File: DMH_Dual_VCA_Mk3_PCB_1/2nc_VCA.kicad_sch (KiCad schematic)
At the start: 51 parts, among them Q5 BC548, Q6 BC548, Q7 BC548, Q8 BC548, SW2 SW_DPDT_3way, U3 TL074, U4 TL072, U7 TL074

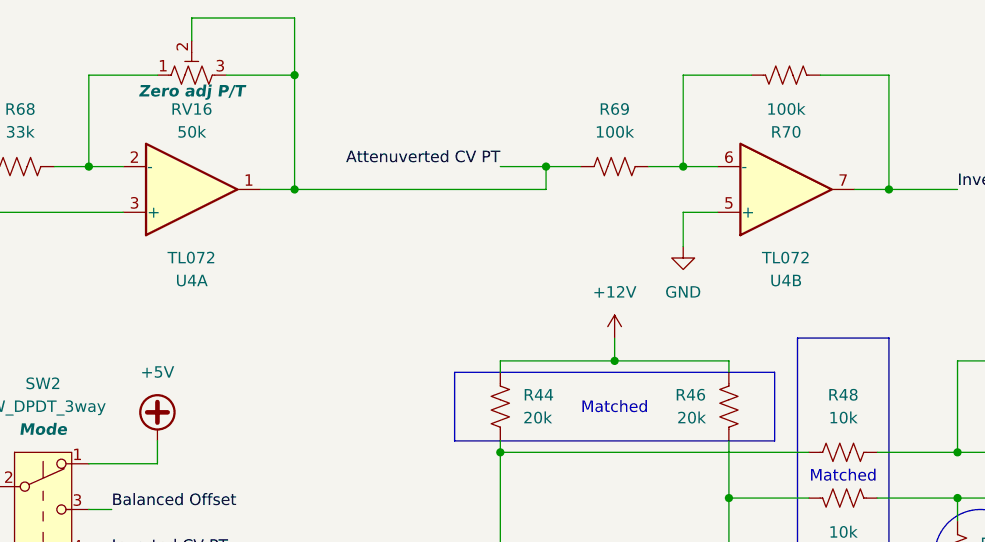
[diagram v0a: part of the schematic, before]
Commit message: Added clipping LED to schematic
Still need to add to Panel
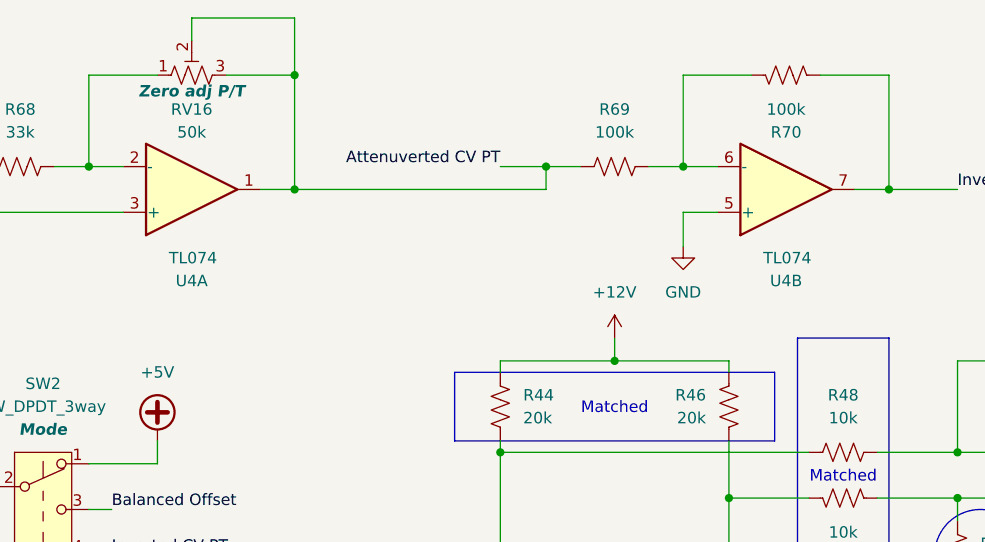
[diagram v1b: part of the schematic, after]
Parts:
- U4: value TL072 -> TL074; footprint Package_DIP:DIP-8_W7.62mm_Socket -> Package_DIP:DIP-14_W7.62mm_Socket; symbol Amplifier_Operational:TL072 -> Amplifier_Operational:TL074
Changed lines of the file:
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@@
 	)
 	(symbol
-		(lib_id "Amplifier_Operational:TL072")
+		(lib_id "Amplifier_Operational:TL074")
 		(at 54.61 31.75 0)
 		(mirror x)
@@
 		(exclude_from_sim no)
 		(in_bom yes)
-		(on_board no)
+		(on_board yes)
 		(dnp no)
 		(property "Reference" "U4"
@@
 			)
 		)
-		(property "Value" "TL072"
-			(at 54.61 39.37 0)
-			(effects
-				(font
-					(size 1.27 1.27)
-				)
-			)
-		)
-		(property "Footprint" "Package_DIP:DIP-8_W7.62mm_Socket"
+		(property "Value" "TL074"
+			(at 52.07 39.37 0)
+			(effects
+				(font
+					(size 1.27 1.27)
+				)
+				(justify left)
+			)
+		)
+		(property "Footprint" "Package_DIP:DIP-14_W7.62mm_Socket"
+			(at 53.34 34.29 0)
+			(effects
+				(font
+					(size 1.27 1.27)
+				)
+				(hide yes)
+			)
+		)
+		(property "Datasheet" "http://www.ti.com/lit/ds/symlink/tl071.pdf"
+			(at 55.88 36.83 0)
+			(effects
+				(font
+					(size 1.27 1.27)
+				)
+				(hide yes)
+			)
+		)
+		(property "Description" "Quad Low-Noise JFET-Input Operational Amplifiers, DIP-14/SOIC-14"
 			(at 54.61 31.75 0)
 			(effects
@@
 			)
 		)
-		(property "Datasheet" "http://www.ti.com/lit/ds/symlink/tl071.pdf"
+		(property "Function" ""
 			(at 54.61 31.75 0)
 			(effects
@@
 					(size 1.27 1.27)
 				)
-				(hide yes)
-			)
-		)
-		(property "Description" "Dual Low-Noise JFET-Input Operational Amplifiers, DIP-8/SOIC-8"
-			(at 54.61 31.75 0)
-			(effects
-				(font
-					(size 1.27 1.27)
-				)
-				(hide yes)
 			)
 		)
@@
 		)
 		(pin "4"
+		)
+		(pin "9"
+		)
+		(pin "10"
+		)
+		(pin "12"
+		)
+		(pin "13"
+		)
+		(pin "14"
+		)
+		(pin "11"
 		)
 		(instances
@@
 	)
 	(symbol
-		(lib_id "Amplifier_Operational:TL072")
+		(lib_id "Amplifier_Operational:TL074")
 		(at 120.65 31.75 0)
 		(mirror x)
@@
 		(exclude_from_sim no)
 		(in_bom yes)
-		(on_board no)
+		(on_board yes)
 		(dnp no)
 		(property "Reference" "U4"
@@
 			)
 		)
-		(property "Value" "TL072"
-			(at 120.65 39.37 0)
-			(effects
-				(font
-					(size 1.27 1.27)
-				)
-			)
-		)
-		(property "Footprint" "Package_DIP:DIP-8_W7.62mm_Socket"
+		(property "Value" "TL074"
+			(at 118.11 39.37 0)
+			(effects
+				(font
+					(size 1.27 1.27)
+				)
+				(justify left)
+			)
+		)
+		(property "Footprint" "Package_DIP:DIP-14_W7.62mm_Socket"
+			(at 119.38 34.29 0)
+			(effects
+				(font
+					(size 1.27 1.27)
+				)
+				(hide yes)
+			)
+		)
+		(property "Datasheet" "http://www.ti.com/lit/ds/symlink/tl071.pdf"
+			(at 121.92 36.83 0)
+			(effects
+				(font
+					(size 1.27 1.27)
+				)
+				(hide yes)
+			)
+		)
+		(property "Description" "Quad Low-Noise JFET-Input Operational Amplifiers, DIP-14/SOIC-14"
 			(at 120.65 31.75 0)
 			(effects
@@
 			)
 		)
-		(property "Datasheet" "http://www.ti.com/lit/ds/symlink/tl071.pdf"
+		(property "Function" ""
 			(at 120.65 31.75 0)
 			(effects
@@
 					(size 1.27 1.27)
 				)
-				(hide yes)
-			)
-		)
-		(property "Description" "Dual Low-Noise JFET-Input Operational Amplifiers, DIP-8/SOIC-8"
-			(at 120.65 31.75 0)
-			(effects
-				(font
-					(size 1.27 1.27)
-				)
-				(hide yes)
 			)
 		)
@@
 		(pin "4"
 		)
-		(instances
+		(pin "13"
+		)
+		(pin "14"
+		)
+		(pin "10"
+		)
+		(pin "9"
+		)
+		(pin "12"
+		)
+		(pin "11"
+		)
+		(instances

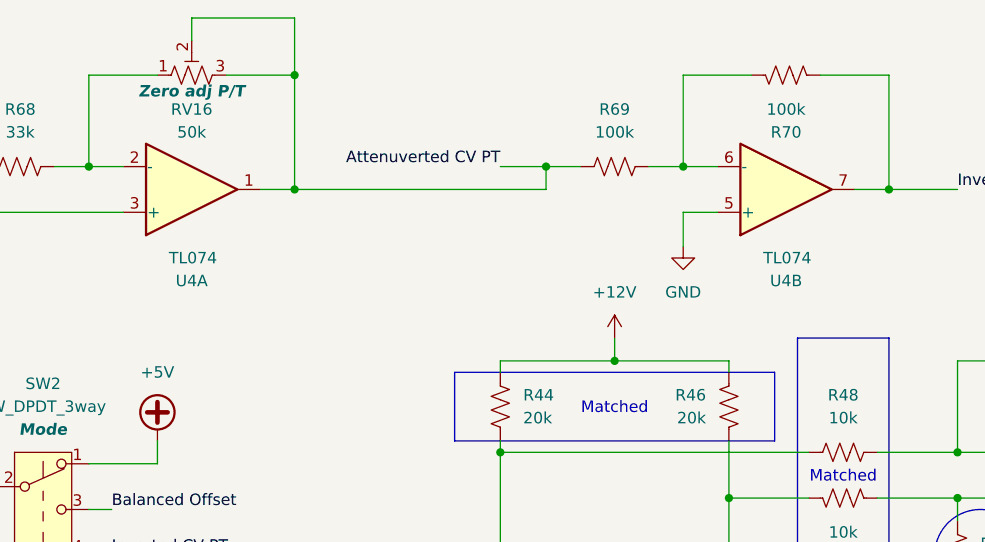
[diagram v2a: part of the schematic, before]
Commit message: Improved clipping indicator
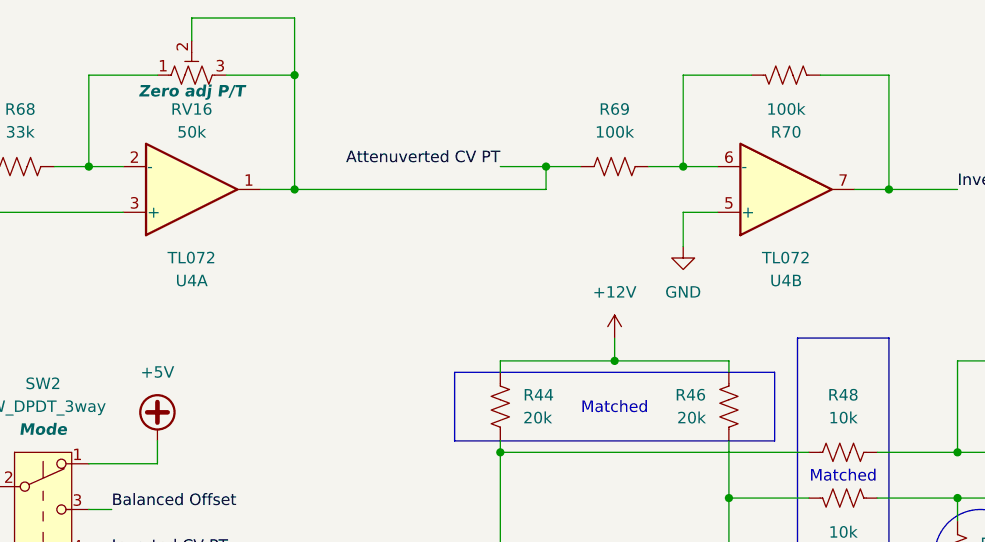
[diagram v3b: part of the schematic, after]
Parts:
- removed U4: TL074, Package_DIP:DIP-14_W7.62mm_Socket, symbol Amplifier_Operational:TL074
- added U4: TL072, Package_DIP:DIP-8_W7.62mm_Socket, symbol Amplifier_Operational:TL072
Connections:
- net Attenuverted CV PT: now also U4.1
- net CV PT Pot G1: now also U4.3 (+)
- net GND: now also U4.5 (+)
- net Inverted CV PT: now also U4.7
- net at R68.2, RV16.1: now also U4.2 (-)
- net at R69.2, R70.1: now also U4.6 (-)
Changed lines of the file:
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@@
-	)
-	(symbol
-		(lib_id "Amplifier_Operational:TL074")
-		(at 54.61 31.75 0)
-		(mirror x)
-		(unit 1)
-		(exclude_from_sim no)
-		(in_bom yes)
-		(on_board no)
-		(dnp no)
-		(property "Reference" "U4"
-			(at 54.61 41.91 0)
-			(effects
-				(font
-					(size 1.27 1.27)
-				)
-			)
-		)
-		(property "Value" "TL074"
-			(at 52.07 39.37 0)
-			(effects
-				(font
-					(size 1.27 1.27)
-				)
-				(justify left)
-			)
-		)
-		(property "Footprint" "Package_DIP:DIP-14_W7.62mm_Socket"
-			(at 53.34 34.29 0)
-			(effects
-				(font
-					(size 1.27 1.27)
-				)
-				(hide yes)
-			)
-		)
-		(property "Datasheet" "http://www.ti.com/lit/ds/symlink/tl071.pdf"
-			(at 55.88 36.83 0)
-			(effects
-				(font
-					(size 1.27 1.27)
-				)
-				(hide yes)
-			)
-		)
-		(property "Description" "Quad Low-Noise JFET-Input Operational Amplifiers, DIP-14/SOIC-14"
-			(at 54.61 31.75 0)
-			(effects
-				(font
-					(size 1.27 1.27)
-				)
-				(hide yes)
-			)
-		)
-		(property "Function" ""
-			(at 54.61 31.75 0)
-			(effects
-				(font
-					(size 1.27 1.27)
-				)
-			)
-		)
-		(pin "1"
-		)
-		(pin "3"
-		)
-		(pin "2"
-		)
-		(pin "6"
-		)
-		(pin "7"
-		)
-		(pin "5"
-		)
-		(pin "8"
-		)
-		(pin "4"
-		)
-		(pin "9"
-		)
-		(pin "10"
-		)
-		(pin "12"
-		)
-		(pin "13"
-		)
-		(pin "14"
-		)
-		(pin "11"
-		)
-		(instances
-			(project ""
-				(path "/58f4306d-5387-4983-bb08-41a2313fd315/8ee005da-7ca8-4d1e-92f5-43ab10d67fe9"
-					(reference "U4")
-					(unit 1)
-				)
-			)
-		)
 	)
 	(symbol
@@
 					(reference "#PWR041")
 					(unit 1)
+				)
+			)
+		)
+	)
+	(symbol
+		(lib_id "Amplifier_Operational:TL072")
+		(at 120.65 31.75 0)
+		(mirror x)
+		(unit 2)
+		(exclude_from_sim no)
+		(in_bom yes)
+		(on_board yes)
+		(dnp no)
+		(property "Reference" "U4"
+			(at 120.65 41.91 0)
+			(effects
+				(font
+					(size 1.27 1.27)
+				)
+			)
+		)
+		(property "Value" "TL072"
+			(at 120.65 39.37 0)
+			(effects
+				(font
+					(size 1.27 1.27)
+				)
+			)
+		)
+		(property "Footprint" "Package_DIP:DIP-8_W7.62mm_Socket"
+			(at 120.65 31.75 0)
+			(effects
+				(font
+					(size 1.27 1.27)
+				)
+				(hide yes)
+			)
+		)
+		(property "Datasheet" "http://www.ti.com/lit/ds/symlink/tl071.pdf"
+			(at 120.65 31.75 0)
+			(effects
+				(font
+					(size 1.27 1.27)
+				)
+				(hide yes)
+			)
+		)
+		(property "Description" "Dual Low-Noise JFET-Input Operational Amplifiers, DIP-8/SOIC-8"
+			(at 120.65 31.75 0)
+			(effects
+				(font
+					(size 1.27 1.27)
+				)
+				(hide yes)
+			)
+		)
+		(pin "6"
+		)
+		(pin "3"
+		)
+		(pin "4"
+		)
+		(pin "2"
+		)
+		(pin "1"
+		)
+		(pin "8"
+		)
+		(pin "7"
+		)
+		(pin "5"
+		)
+		(instances
+			(project ""
+				(path "/58f4306d-5387-4983-bb08-41a2313fd315/8ee005da-7ca8-4d1e-92f5-43ab10d67fe9"
+					(reference "U4")
+					(unit 2)
 				)
 			)
@@
 	)
 	(symbol
-		(lib_id "Amplifier_Operational:TL074")
-		(at 120.65 31.75 0)
-		(mirror x)
-		(unit 2)
-		(exclude_from_sim no)
-		(in_bom yes)
-		(on_board no)
-		(dnp no)
-		(property "Reference" "U4"
-			(at 120.65 41.91 0)
-			(effects
-				(font
-					(size 1.27 1.27)
-				)
-			)
-		)
-		(property "Value" "TL074"
-			(at 118.11 39.37 0)
-			(effects
-				(font
-					(size 1.27 1.27)
-				)
-				(justify left)
-			)
-		)
-		(property "Footprint" "Package_DIP:DIP-14_W7.62mm_Socket"
-			(at 119.38 34.29 0)
-			(effects
-				(font
-					(size 1.27 1.27)
-				)
-				(hide yes)
-			)
-		)
-		(property "Datasheet" "http://www.ti.com/lit/ds/symlink/tl071.pdf"
-			(at 121.92 36.83 0)
-			(effects
-				(font
-					(size 1.27 1.27)
-				)
-				(hide yes)
-			)
-		)
-		(property "Description" "Quad Low-Noise JFET-Input Operational Amplifiers, DIP-14/SOIC-14"
-			(at 120.65 31.75 0)
-			(effects
-				(font
-					(size 1.27 1.27)
-				)
-				(hide yes)
-			)
-		)
-		(property "Function" ""
-			(at 120.65 31.75 0)
-			(effects
-				(font
-					(size 1.27 1.27)
-				)
-			)
-		)
-		(pin "1"
-		)
-		(pin "3"
-		)
-		(pin "2"
-		)
-		(pin "6"
-		)
-		(pin "7"
-		)
-		(pin "5"
-		)
-		(pin "8"
-		)
-		(pin "4"
-		)
-		(pin "13"
-		)
-		(pin "14"
-		)
-		(pin "10"
-		)
-		(pin "9"
-		)
-		(pin "12"
-		)
-		(pin "11"
-		)
-		(instances
-			(project ""
-				(path "/58f4306d-5387-4983-bb08-41a2313fd315/8ee005da-7ca8-4d1e-92f5-43ab10d67fe9"
-					(reference "U4")
-					(unit 2)
-				)
-			)
-		)
-	)
-	(symbol
 		(lib_id "Device:R_US")
 		(at 127 171.45 180)
@@
 					(unit 1)
 				)
+			)
+		)
+	)
+	(symbol
+		(lib_id "Amplifier_Operational:TL072")
+		(at 54.61 31.75 0)
+		(mirror x)
+		(unit 1)
+		(exclude_from_sim no)
+		(in_bom yes)
+		(on_board yes)
+		(dnp no)
+		(property "Reference" "U4"
+			(at 54.61 41.91 0)
+			(effects
+				(font
+					(size 1.27 1.27)
+				)
+			)
+		)
+		(property "Value" "TL072"
+			(at 54.61 39.37 0)
+			(effects
+				(font
+					(size 1.27 1.27)
+				)
+			)
+		)
+		(property "Footprint" "Package_DIP:DIP-8_W7.62mm_Socket"
+			(at 54.61 31.75 0)
+			(effects
+				(font
+					(size 1.27 1.27)
+				)
+				(hide yes)
+			)
+		)
+		(property "Datasheet" "http://www.ti.com/lit/ds/symlink/tl071.pdf"
+			(at 54.61 31.75 0)
+			(effects
+				(font
+					(size 1.27 1.27)
+				)
+				(hide yes)
+			)
+		)
+		(property "Description" "Dual Low-Noise JFET-Input Operational Amplifiers, DIP-8/SOIC-8"
+			(at 54.61 31.75 0)
+			(effects
+				(font
+					(size 1.27 1.27)
+				)
+				(hide yes)
+			)
+		)
+		(pin "6"
+		)
+		(pin "3"
+		)
+		(pin "4"
+		)
+		(pin "2"
+		)
+		(pin "1"
+		)
+		(pin "8"
+		)
+		(pin "7"
+		)
+		(pin "5"
+		)
+		(instances
+			(project ""
+				(path "/58f4306d-5387-4983-bb08-41a2313fd315/8ee005da-7ca8-4d1e-92f5-43ab10d67fe9"
+					(reference "U4")
+					(unit 1)
+				)
